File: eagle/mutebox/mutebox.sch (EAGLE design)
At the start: 58 parts, among them IC1 74HCT595D, IC2 74HC165D

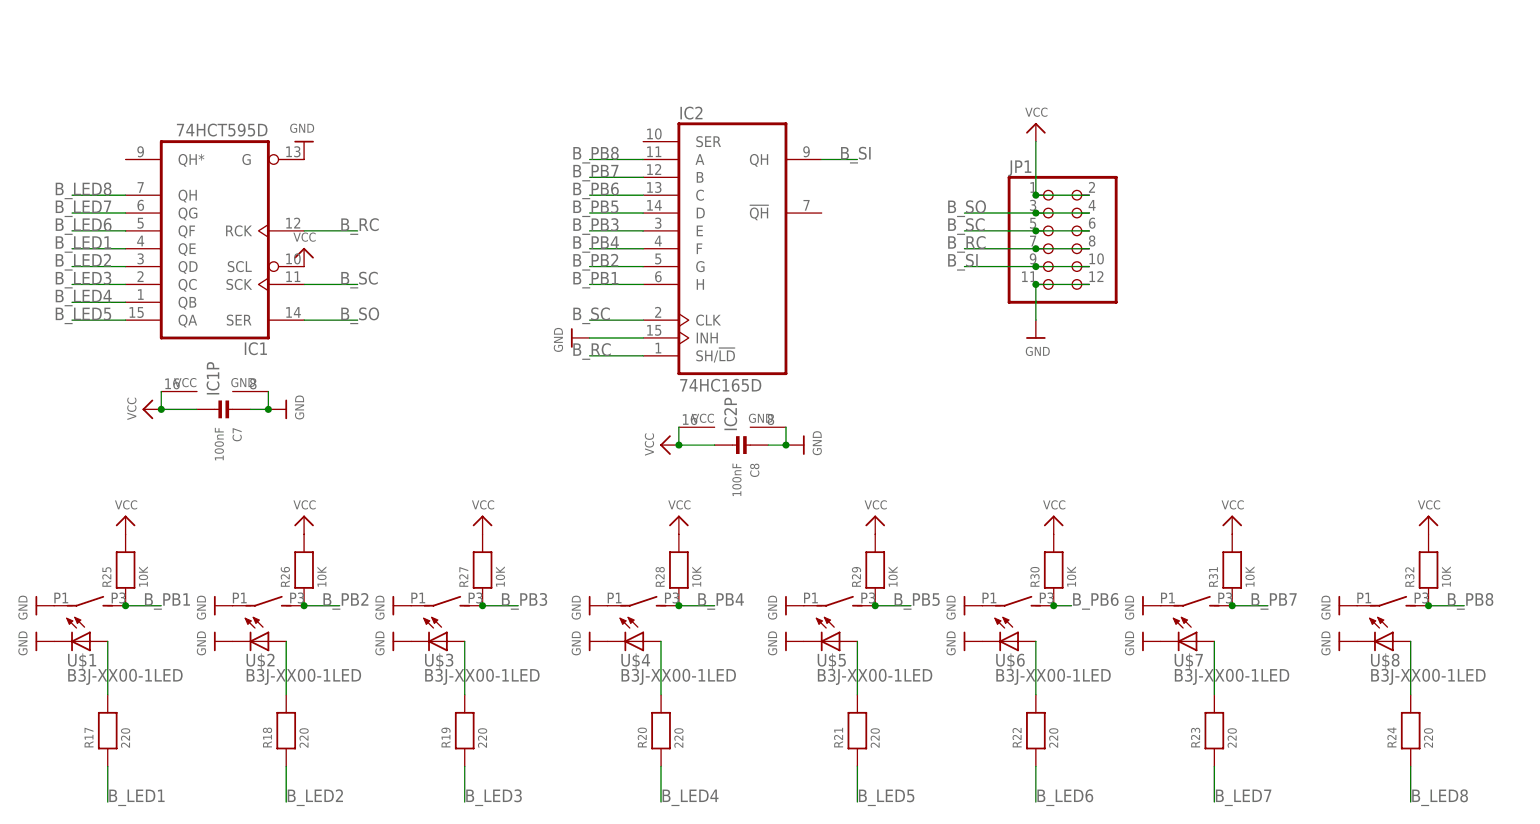
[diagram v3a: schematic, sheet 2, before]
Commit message: mutebox: connectors now match midibox
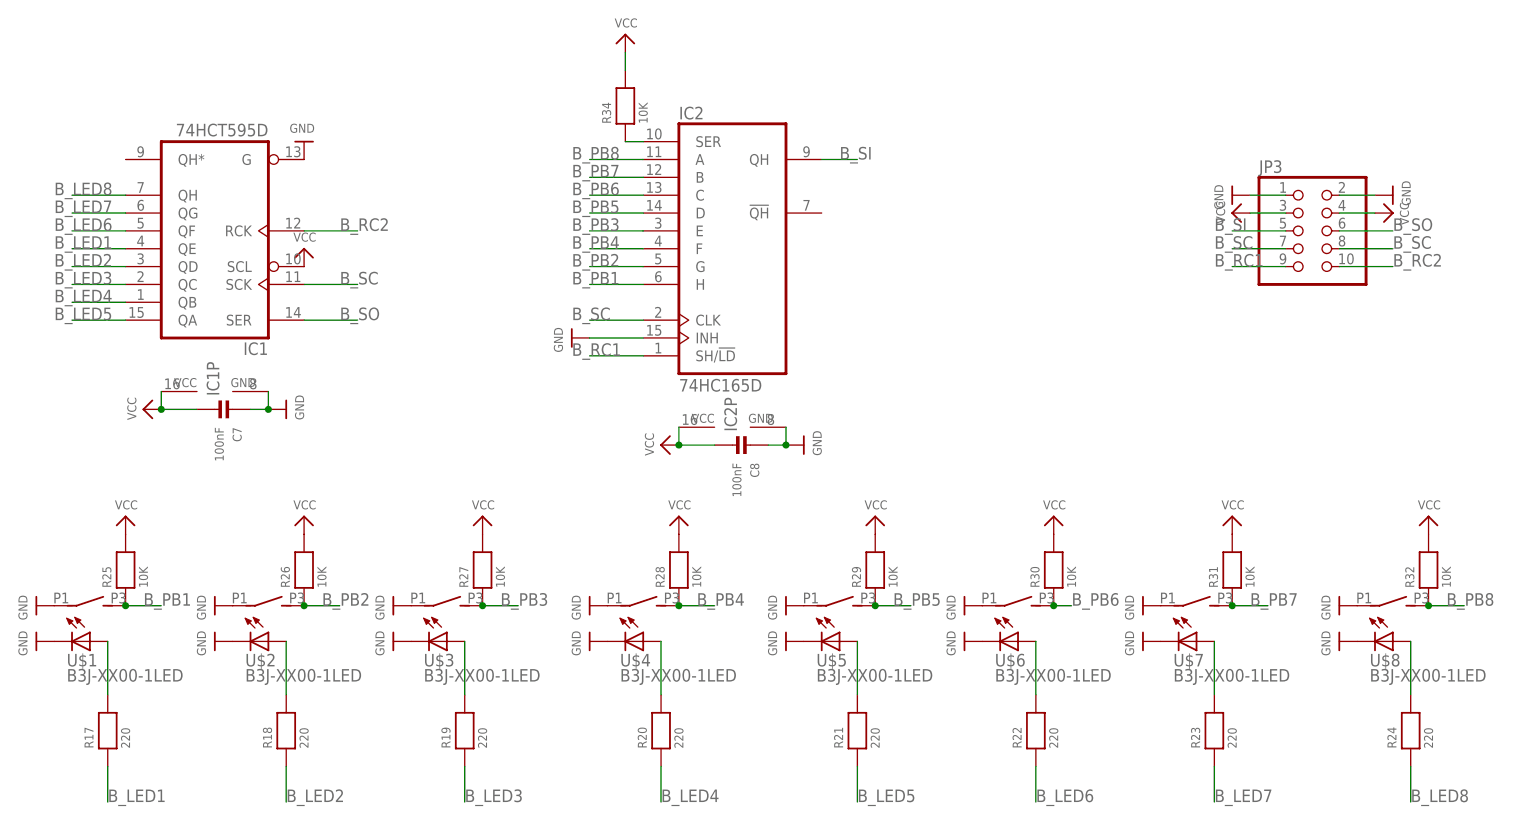
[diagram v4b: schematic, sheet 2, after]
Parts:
- removed JP1, JP4: (no value), pinhead:PINHD-2X6
- added JP2, JP3: (no value), pinhead:PINHD-2X5
- added R33: 10, microbuilder:RESISTOR_0805
- added R34: 10K, microbuilder:RESISTOR_0603
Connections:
- removed net B_RC: IC1A.RCK, IC2A.SH/!LD, JP1.7, JP1.8
- new net B_RC1: IC2A.SH/!LD, JP3.9
- new net B_RC2: IC1A.RCK, JP3.10
- new net N$10: IC2A.SER, R34.1
- new net N$9: JP2.3, JP2.4, R33.1
- net AGND: now also JP2.1, JP2.2; no longer JP4.11, JP4.12
- net AVCC: now also R33.2; no longer JP4.1, JP4.2
- net B_SC: now also JP3.7, JP3.8; no longer JP1.5, JP1.6
- net B_SI: now also JP3.5; no longer JP1.10, JP1.9
- net B_SO: now also JP3.6; no longer JP1.3, JP1.4
- net GND: now also JP3.1, JP3.2; no longer JP1.11, JP1.12
- net P_CLK: now also JP2.7, JP2.8; no longer JP4.7, JP4.8
- net P_CS1: now also JP2.10; no longer JP4.4
- net P_CS2: now also JP2.9; no longer JP4.3
- net P_DIN: now also JP2.6; no longer JP4.6
- net P_DOUT: now also JP2.5; no longer JP4.5
- net VCC: now also JP3.3, JP3.4, R34.2; no longer JP1.1, JP1.2

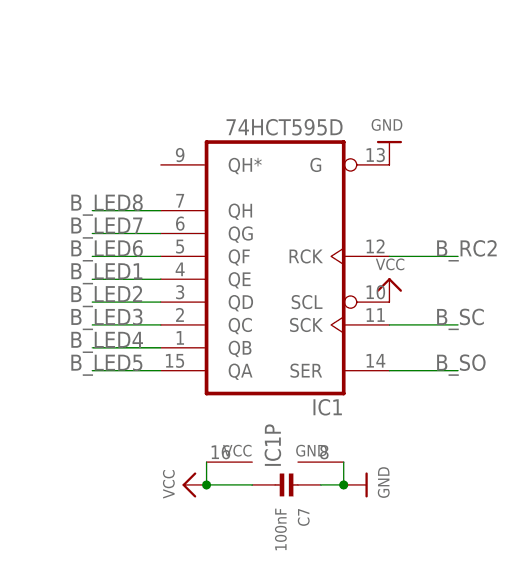
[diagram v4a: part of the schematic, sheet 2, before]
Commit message: mutebox: rearranged leds
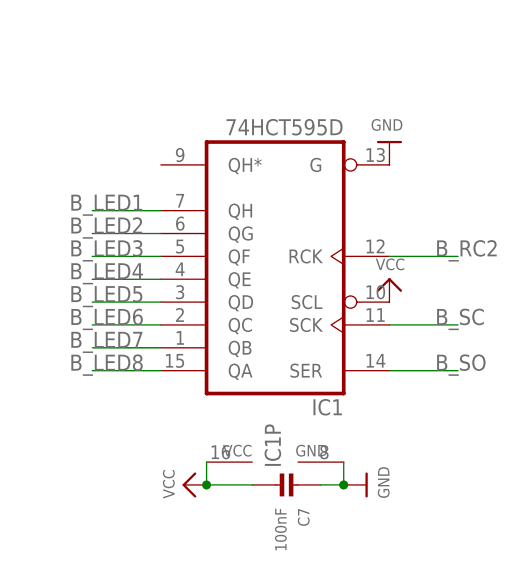
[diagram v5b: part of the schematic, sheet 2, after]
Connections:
- net B_LED1: now also IC1A.QH; no longer IC1A.QE
- net B_LED2: now also IC1A.QG; no longer IC1A.QD
- net B_LED3: now also IC1A.QF; no longer IC1A.QC
- net B_LED4: now also IC1A.QE; no longer IC1A.QB
- net B_LED5: now also IC1A.QD; no longer IC1A.QA
- net B_LED6: now also IC1A.QC; no longer IC1A.QF
- net B_LED7: now also IC1A.QB; no longer IC1A.QG
- net B_LED8: now also IC1A.QA; no longer IC1A.QH
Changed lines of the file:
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@@
 <segment>
 <pinref part="R33" gate="G$1" pin="1"/>
+<wire x1="43.18" y1="20.32" x2="25.4" y2="20.32" width="0.1524" layer="91"/>
 <pinref part="JP2" gate="A" pin="4"/>
-<wire x1="43.18" y1="20.32" x2="27.94" y2="20.32" width="0.1524" layer="91"/>
 <pinref part="JP2" gate="A" pin="3"/>
 <wire x1="17.78" y1="20.32" x2="25.4" y2="20.32" width="0.1524" layer="91"/>
-<wire x1="25.4" y1="20.32" x2="27.94" y2="20.32" width="0.1524" layer="91"/>
-<junction x="27.94" y="20.32"/>
+<junction x="25.4" y="20.32"/>
 </segment>
 </net>
@@
 </segment>
 <segment>
+<pinref part="IC1" gate="A" pin="QH"/>
+<wire x1="15.24" y1="66.04" x2="7.62" y2="66.04" width="0.1524" layer="91"/>
+<label x="5.08" y="66.04" size="1.778" layer="95"/>
+</segment>
+</net>
+<net name="B_LED2" class="0">
+<segment>
+<pinref part="R18" gate="G$1" pin="1"/>
+<wire x1="38.1" y1="-15.24" x2="38.1" y2="-20.32" width="0.1524" layer="91"/>
+<label x="38.1" y="-20.32" size="1.778" layer="95"/>
+</segment>
+<segment>
+<pinref part="IC1" gate="A" pin="QG"/>
+<wire x1="15.24" y1="63.5" x2="7.62" y2="63.5" width="0.1524" layer="91"/>
+<label x="5.08" y="63.5" size="1.778" layer="95"/>
+</segment>
+</net>
+<net name="B_LED3" class="0">
+<segment>
+<pinref part="R19" gate="G$1" pin="1"/>
+<wire x1="63.5" y1="-15.24" x2="63.5" y2="-20.32" width="0.1524" layer="91"/>
+<label x="63.5" y="-20.32" size="1.778" layer="95"/>
+</segment>
+<segment>
+<pinref part="IC1" gate="A" pin="QF"/>
+<wire x1="15.24" y1="60.96" x2="7.62" y2="60.96" width="0.1524" layer="91"/>
+<label x="5.08" y="60.96" size="1.778" layer="95"/>
+</segment>
+</net>
+<net name="B_LED4" class="0">
+<segment>
+<pinref part="R20" gate="G$1" pin="1"/>
+<wire x1="91.44" y1="-15.24" x2="91.44" y2="-20.32" width="0.1524" layer="91"/>
+<label x="91.44" y="-20.32" size="1.778" layer="95"/>
+</segment>
+<segment>
 <pinref part="IC1" gate="A" pin="QE"/>
 <wire x1="15.24" y1="58.42" x2="7.62" y2="58.42" width="0.1524" layer="91"/>
@@
 </segment>
 </net>
-<net name="B_LED2" class="0">
-<segment>
-<pinref part="R18" gate="G$1" pin="1"/>
-<wire x1="38.1" y1="-15.24" x2="38.1" y2="-20.32" width="0.1524" layer="91"/>
-<label x="38.1" y="-20.32" size="1.778" layer="95"/>
+<net name="B_LED5" class="0">
+<segment>
+<pinref part="R21" gate="G$1" pin="1"/>
+<wire x1="119.38" y1="-15.24" x2="119.38" y2="-20.32" width="0.1524" layer="91"/>
+<label x="119.38" y="-20.32" size="1.778" layer="95"/>
 </segment>
 <segment>
@@
 </segment>
 </net>
-<net name="B_LED3" class="0">
-<segment>
-<pinref part="R19" gate="G$1" pin="1"/>
-<wire x1="63.5" y1="-15.24" x2="63.5" y2="-20.32" width="0.1524" layer="91"/>
-<label x="63.5" y="-20.32" size="1.778" layer="95"/>
+<net name="B_LED6" class="0">
+<segment>
+<pinref part="R22" gate="G$1" pin="1"/>
+<wire x1="144.78" y1="-15.24" x2="144.78" y2="-20.32" width="0.1524" layer="91"/>
+<label x="144.78" y="-20.32" size="1.778" layer="95"/>
 </segment>
 <segment>
@@
 </segment>
 </net>
-<net name="B_LED4" class="0">
-<segment>
-<pinref part="R20" gate="G$1" pin="1"/>
-<wire x1="91.44" y1="-15.24" x2="91.44" y2="-20.32" width="0.1524" layer="91"/>
-<label x="91.44" y="-20.32" size="1.778" layer="95"/>
+<net name="B_LED7" class="0">
+<segment>
+<pinref part="R23" gate="G$1" pin="1"/>
+<wire x1="170.18" y1="-15.24" x2="170.18" y2="-20.32" width="0.1524" layer="91"/>
+<label x="170.18" y="-20.32" size="1.778" layer="95"/>
 </segment>
 <segment>
@@
 </segment>
 </net>
-<net name="B_LED5" class="0">
-<segment>
-<pinref part="R21" gate="G$1" pin="1"/>
-<wire x1="119.38" y1="-15.24" x2="119.38" y2="-20.32" width="0.1524" layer="91"/>
-<label x="119.38" y="-20.32" size="1.778" layer="95"/>
+<net name="B_LED8" class="0">
+<segment>
+<pinref part="R24" gate="G$1" pin="1"/>
+<wire x1="198.12" y1="-15.24" x2="198.12" y2="-20.32" width="0.1524" layer="91"/>
+<label x="198.12" y="-20.32" size="1.778" layer="95"/>
 </segment>
 <segment>
@@
 </segment>
 </net>
-<net name="B_LED6" class="0">
-<segment>
-<pinref part="R22" gate="G$1" pin="1"/>
-<wire x1="144.78" y1="-15.24" x2="144.78" y2="-20.32" width="0.1524" layer="91"/>
-<label x="144.78" y="-20.32" size="1.778" layer="95"/>
-</segment>
-<segment>
-<pinref part="IC1" gate="A" pin="QF"/>
-<wire x1="15.24" y1="60.96" x2="7.62" y2="60.96" width="0.1524" layer="91"/>
-<label x="5.08" y="60.96" size="1.778" layer="95"/>
-</segment>
-</net>
-<net name="B_LED7" class="0">
-<segment>
-<pinref part="R23" gate="G$1" pin="1"/>
-<wire x1="170.18" y1="-15.24" x2="170.18" y2="-20.32" width="0.1524" layer="91"/>
-<label x="170.18" y="-20.32" size="1.778" layer="95"/>
-</segment>
-<segment>
-<pinref part="IC1" gate="A" pin="QG"/>
-<wire x1="15.24" y1="63.5" x2="7.62" y2="63.5" width="0.1524" layer="91"/>
-<label x="5.08" y="63.5" size="1.778" layer="95"/>
-</segment>
-</net>
-<net name="B_LED8" class="0">
-<segment>
-<pinref part="R24" gate="G$1" pin="1"/>
-<wire x1="198.12" y1="-15.24" x2="198.12" y2="-20.32" width="0.1524" layer="91"/>
-<label x="198.12" y="-20.32" size="1.778" layer="95"/>
-</segment>
-<segment>
-<pinref part="IC1" gate="A" pin="QH"/>
-<wire x1="15.24" y1="66.04" x2="7.62" y2="66.04" width="0.1524" layer="91"/>
-<label x="5.08" y="66.04" size="1.778" layer="95"/>
-</segment>
-</net>

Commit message: mutebox
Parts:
- IC3, IC4: value 21298E -> MCP3208
- renumbered JP2 to P_CONN, JP3 to B_CONN, U$29 to IC3, U$47 to IC4
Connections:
- net B_PB3: now also IC2A.F; no longer IC2A.E
- net B_PB4: now also IC2A.E; no longer IC2A.F
- net P10: now also IC3.CH2; no longer IC3.CH3
- net P11: now also IC3.CH1; no longer IC3.CH4
- net P12: now also IC3.CH0; no longer IC3.CH1
- net P15: now also IC4.CH2; no longer IC4.CH3
- net P16: now also IC4.CH0; no longer IC4.CH1
- net P2: now also IC3.CH6; no longer IC3.CH5
- net P3: now also IC3.CH5; no longer IC3.CH2
- net P4: now also IC3.CH4; no longer IC3.CH0
- net P7: now also IC4.CH3; no longer IC4.CH2
- net P8: now also IC4.CH1; no longer IC4.CH0
- net P9: now also IC3.CH3; no longer IC3.CH6

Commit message: wip
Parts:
- R1: value 10kB -> 10kB (688-RK09D1130C2P)
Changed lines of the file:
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@@
 <part name="U$6" library="keves" deviceset="B3J-XX00-1LED" device=""/>
 <part name="U$1" library="keves" deviceset="B3J-XX00-1LED" device=""/>
-<part name="R1" library="pot-alps" deviceset="POT_US" device="VERTICAL_PS" value="10kB"/>
+<part name="R1" library="pot-alps" deviceset="POT_US" device="VERTICAL_PS" value="10kB (688-RK09D1130C2P)"/>
 <part name="R12" library="pot-alps" deviceset="POT_US" device="VERTICAL_PS" value="10kB"/>
 <part name="R10" library="pot-alps" deviceset="POT_US" device="VERTICAL_PS" value="10kB"/>

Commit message: muteboxwip
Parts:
- B_CONN, P_CONN: device pinhead:PINHD-2X5 -> microbuilder:HEADER-2X5
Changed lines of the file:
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@@
 <part name="U$9" library="microbuilder" deviceset="AGND" device=""/>
 <part name="U$10" library="microbuilder" deviceset="AGND" device=""/>
-<part name="P_CONN" library="pinhead" deviceset="PINHD-2X5" device=""/>
+<part name="P_CONN" library="microbuilder" deviceset="HEADER-2X5" device=""/>
 <part name="R33" library="microbuilder" deviceset="RESISTOR" device="_0805" value="10"/>
 <part name="U$27" library="microbuilder" deviceset="AVCC" device=""/>
-<part name="B_CONN" library="pinhead" deviceset="PINHD-2X5" device=""/>
+<part name="B_CONN" library="microbuilder" deviceset="HEADER-2X5" device=""/>
 <part name="U$28" library="microbuilder" deviceset="GND" device=""/>
 <part name="U$78" library="microbuilder" deviceset="GND" device=""/>
